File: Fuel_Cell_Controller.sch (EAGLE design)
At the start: 93 parts, among them J1 BLUETOOTH, U1 MAX232PTH

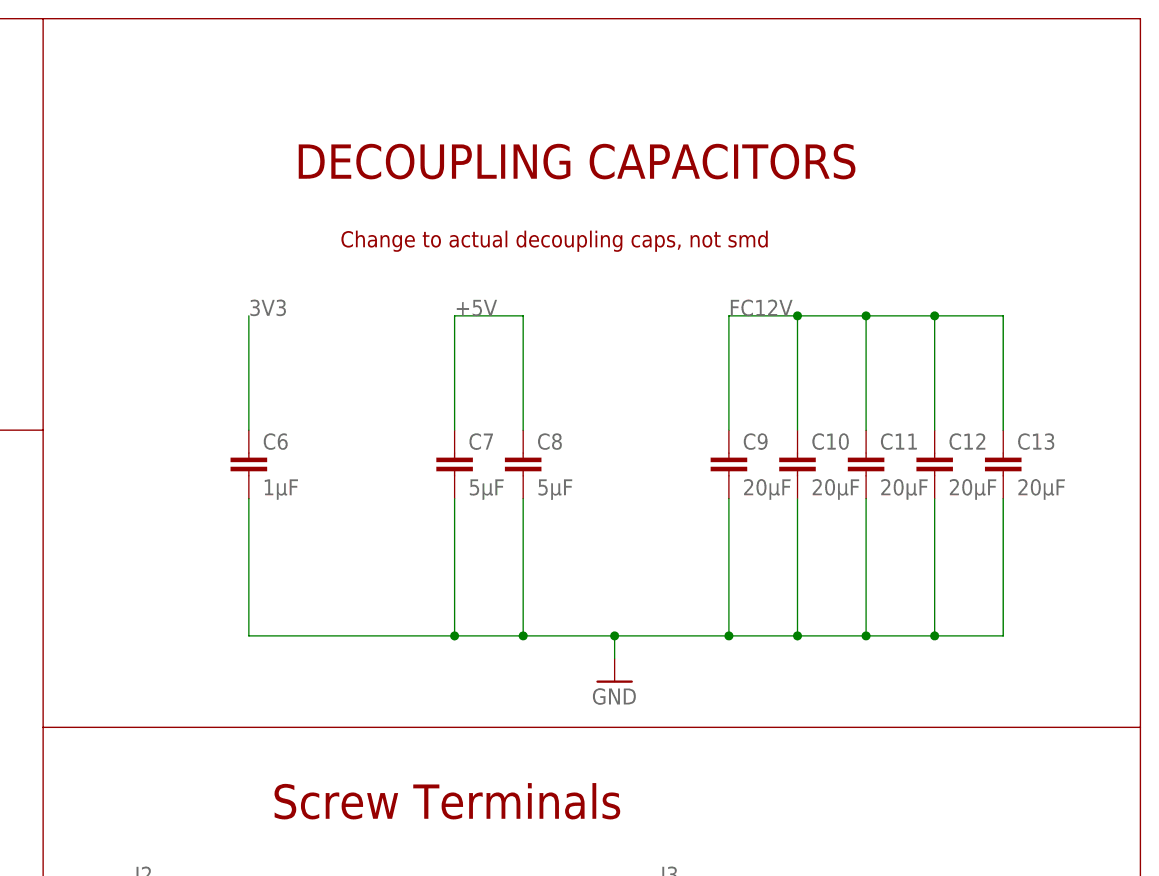
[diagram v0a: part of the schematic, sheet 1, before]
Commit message: Changed the values and number of decoupling capacitors
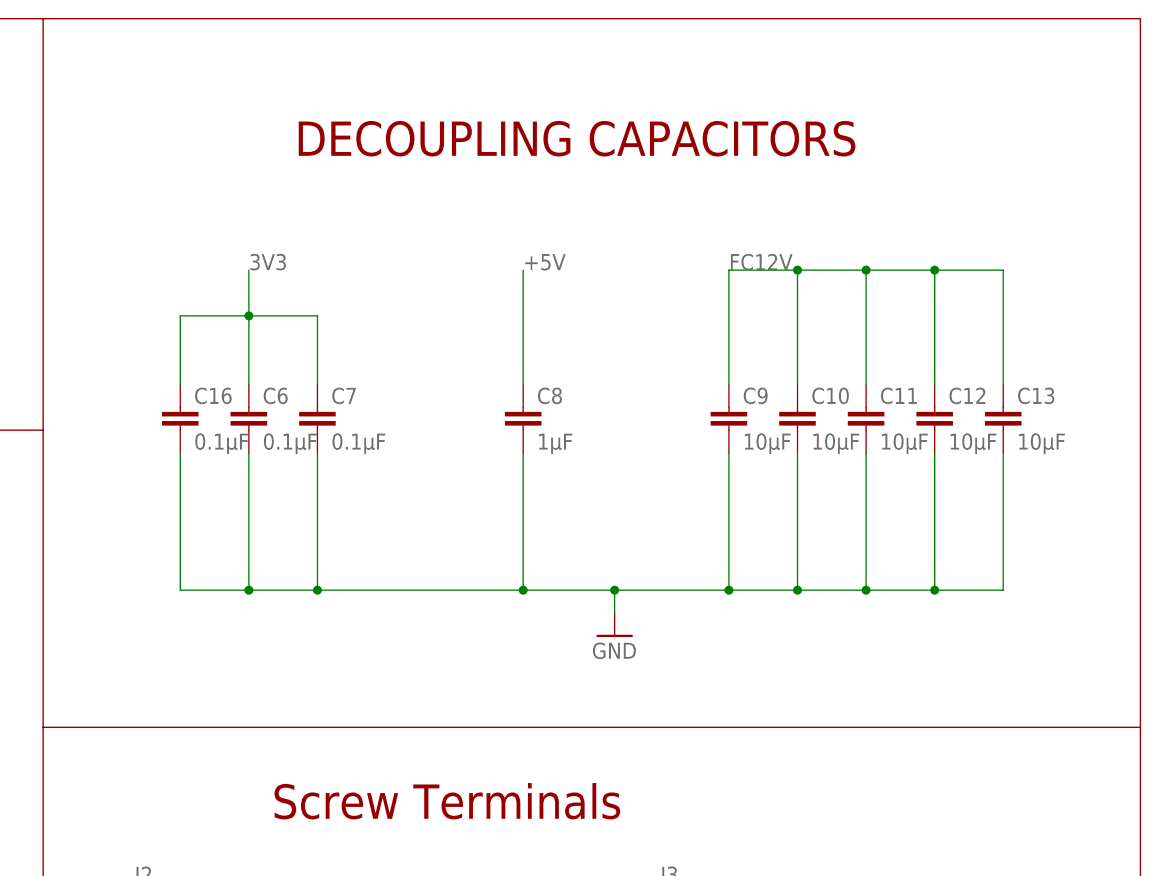
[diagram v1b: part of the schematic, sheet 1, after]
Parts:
- added C16: 0.1µF, SparkFun-Capacitors:CAP0805
- C10, C11, C12, C13, C9: value 20µF -> 10µF; device SparkFun-Capacitors:CAP0603-CAP -> SparkFun-Capacitors:CAP0805
- C6: value 1µF -> 0.1µF; device SparkFun-Capacitors:CAP0603-CAP -> SparkFun-Capacitors:CAP0805
- C7: value 5µF -> 0.1µF; device SparkFun-Capacitors:CAP0603-CAP -> SparkFun-Capacitors:CAP0805
- C8: value 5µF -> 1µF; device SparkFun-Capacitors:CAP0603-CAP -> SparkFun-Capacitors:CAP0805
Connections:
- net +5V: no longer C7.1
- net 3V3: now also C16.1, C7.1
- net GND: now also C16.2
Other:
- note removed: "Change to actual decoupling caps, not smd"
- moved on the sheet: C10, C11, C12, C13, C6, C7, C8, C9

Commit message: Added push button
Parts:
- added R24: 10kΩ, SparkFun-Passives:RESISTOR0805-RES
- added U$26: EG4621CT-ND, EG4621CT-ND:EG4621CT-ND
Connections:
- new net BUTTON: R24.2, U$1.PF_2, U$26.P$2
- net 3V3: now also U$26.P$1
- net GND: now also R24.1
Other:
- note added: "PUSH BUTTON (ACTIVE HIGH)"
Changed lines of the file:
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@@
 <part name="C7" library="SparkFun-Capacitors" deviceset="CAP" device="0805" value="0.1µF"/>
 <part name="C16" library="SparkFun-Capacitors" deviceset="CAP" device="0805" value="0.1µF"/>
+<part name="U$26" library="EG4621CT-ND" deviceset="EG4621CT-ND" device=""/>
+<part name="R24" library="SparkFun-Passives" deviceset="RESISTOR" device="0805-RES" value="10kΩ"/>
 </parts>
 <sheets>
@@
 <wire x1="256.54" y1="-180.34" x2="256.54" y2="-96.52" width="0.1524" layer="94"/>
 <text x="287.02" y="-147.32" size="3.81" layer="94">Indicator LED's</text>
-<wire x1="360.68" y1="-215.9" x2="360.68" y2="-137.16" width="0.1524" layer="94"/>
+<wire x1="360.68" y1="-215.9" x2="360.68" y2="-172.72" width="0.1524" layer="94"/>
+<wire x1="360.68" y1="-172.72" x2="360.68" y2="-137.16" width="0.1524" layer="94"/>
 <wire x1="-93.98" y1="-208.28" x2="-93.98" y2="-259.08" width="0.1524" layer="94"/>
 <wire x1="-93.98" y1="-259.08" x2="124.46" y2="-259.08" width="0.1524" layer="94"/>
@@
 <wire x1="482.6" y1="-45.72" x2="482.6" y2="-127" width="0.1524" layer="94"/>
 <wire x1="482.6" y1="-127" x2="360.68" y2="-127" width="0.1524" layer="94"/>
+<text x="383.54" y="-137.16" size="3.81" layer="94">PUSH BUTTON (ACTIVE HIGH)</text>
+<wire x1="360.68" y1="-172.72" x2="482.6" y2="-172.72" width="0.1524" layer="94"/>
+<wire x1="482.6" y1="-172.72" x2="482.6" y2="-127" width="0.1524" layer="94"/>
 </plain>
 <instances>
@@
 <instance part="C7" gate="G$1" x="391.16" y="33.02"/>
 <instance part="C16" gate="G$1" x="375.92" y="33.02"/>
+<instance part="U$26" gate="G$1" x="408.94" y="-154.94"/>
+<instance part="R24" gate="G$1" x="411.48" y="-162.56"/>
 </instances>
 <busses>
@@
 <label x="447.04" y="-30.48" size="1.778" layer="95"/>
 </segment>
+<segment>
+<pinref part="R24" gate="G$1" pin="1"/>
+<wire x1="406.4" y1="-162.56" x2="388.62" y2="-162.56" width="0.1524" layer="91"/>
+<label x="388.62" y="-162.56" size="1.778" layer="95"/>
+</segment>
 </net>
 <net name="+5V" class="0">
@@
 <pinref part="R16" gate="G$1" pin="1"/>
 <wire x1="-50.8" y1="-165.1" x2="-38.1" y2="-165.1" width="0.1524" layer="91"/>
+</segment>
+<segment>
+<pinref part="U$26" gate="G$1" pin="P$1"/>
+<wire x1="401.32" y1="-154.94" x2="388.62" y2="-154.94" width="0.1524" layer="91"/>
+<label x="388.62" y="-154.94" size="1.778" layer="95"/>
 </segment>
 </net>
@@
 </segment>
 </net>
+<net name="BUTTON" class="0">
+<segment>
+<pinref part="U$26" gate="G$1" pin="P$2"/>
+<label x="424.18" y="-154.94" size="1.778" layer="95"/>
+<wire x1="416.56" y1="-154.94" x2="419.1" y2="-154.94" width="0.1524" layer="91"/>
+<pinref part="R24" gate="G$1" pin="2"/>
+<wire x1="419.1" y1="-154.94" x2="429.26" y2="-154.94" width="0.1524" layer="91"/>
+<wire x1="419.1" y1="-154.94" x2="419.1" y2="-162.56" width="0.1524" layer="91"/>
+<wire x1="419.1" y1="-162.56" x2="416.56" y2="-162.56" width="0.1524" layer="91"/>
+<junction x="419.1" y="-154.94"/>
+</segment>
+<segment>
+<pinref part="U$1" gate="G$1" pin="PF_2"/>
+<wire x1="88.9" y1="-17.78" x2="109.22" y2="-17.78" width="0.1524" layer="91"/>
+<label x="104.14" y="-17.78" size="1.778" layer="95"/>
+</segment>
+</net>

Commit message: Added electrolytic decoupling capacitors and start signal
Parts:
- added ETH9: ETHERNET, ETHERNET:ETHERNET
- added JP4: (no value), jumper:JP1E
- added U$27, U$28: 1µF, 100uF_Cap:CAP-VS-SERIES-PACKAGE-E(ELECT)VS-SERIES-PACKAGE-E
- added U$29: 10µF, 100uF_Cap:CAP-VS-SERIES-PACKAGE-E(ELECT)VS-SERIES-PACKAGE-E
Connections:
- new net START: J3.5, JP4.2
- new net _START: ETH9.1, JP4.1, U$1.PF_12(D8)
- net +5V: now also U$28.+
- net 3V3: now also U$27.+
- net FC12V: now also U$29.+
- net GND: now also ETH9.8, ETH9.SHD1, ETH9.SHD2, U$27.-, U$28.-, U$29.-
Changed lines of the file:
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@@
 <part name="U$26" library="EG4621CT-ND" deviceset="EG4621CT-ND" device=""/>
 <part name="R24" library="SparkFun-Passives" deviceset="RESISTOR" device="0805-RES" value="10kΩ"/>
+<part name="U$27" library="100uF_Cap" deviceset="CAP-VS-SERIES-PACKAGE-E(ELECT)" device="VS-SERIES-PACKAGE-E" value="1µF"/>
+<part name="U$28" library="100uF_Cap" deviceset="CAP-VS-SERIES-PACKAGE-E(ELECT)" device="VS-SERIES-PACKAGE-E" value="1µF"/>
+<part name="U$29" library="100uF_Cap" deviceset="CAP-VS-SERIES-PACKAGE-E(ELECT)" device="VS-SERIES-PACKAGE-E" value="10µF"/>
+<part name="JP4" library="jumper" library_urn="urn:adsk.eagle:library:252" deviceset="JP1E" device="" package3d_urn="urn:adsk.eagle:package:15455/1"/>
+<part name="ETH9" library="ETHERNET" deviceset="ETHERNET" device=""/>
 </parts>
 <sheets>
@@
 <instance part="U$26" gate="G$1" x="408.94" y="-154.94"/>
 <instance part="R24" gate="G$1" x="411.48" y="-162.56"/>
+<instance part="U$27" gate="G$1" x="398.78" y="35.56"/>
+<instance part="U$28" gate="G$1" x="421.64" y="35.56"/>
+<instance part="U$29" gate="G$1" x="474.98" y="35.56"/>
+<instance part="JP4" gate="A" x="421.64" y="-40.64" rot="R90"/>
 </instances>
 <busses>
@@
 <wire x1="467.36" y1="30.48" x2="467.36" y2="15.24" width="0.1524" layer="91"/>
 <wire x1="383.54" y1="15.24" x2="391.16" y2="15.24" width="0.1524" layer="91"/>
-<wire x1="391.16" y1="15.24" x2="414.02" y2="15.24" width="0.1524" layer="91"/>
-<wire x1="414.02" y1="15.24" x2="424.18" y2="15.24" width="0.1524" layer="91"/>
+<wire x1="391.16" y1="15.24" x2="398.78" y2="15.24" width="0.1524" layer="91"/>
+<wire x1="398.78" y1="15.24" x2="414.02" y2="15.24" width="0.1524" layer="91"/>
+<wire x1="414.02" y1="15.24" x2="421.64" y2="15.24" width="0.1524" layer="91"/>
+<wire x1="421.64" y1="15.24" x2="424.18" y2="15.24" width="0.1524" layer="91"/>
 <wire x1="424.18" y1="15.24" x2="436.88" y2="15.24" width="0.1524" layer="91"/>
 <wire x1="436.88" y1="15.24" x2="444.5" y2="15.24" width="0.1524" layer="91"/>
@@
 <wire x1="375.92" y1="15.24" x2="375.92" y2="30.48" width="0.1524" layer="91"/>
 <junction x="383.54" y="15.24"/>
+<pinref part="U$27" gate="G$1" pin="-"/>
+<wire x1="398.78" y1="30.48" x2="398.78" y2="15.24" width="0.1524" layer="91"/>
+<junction x="398.78" y="15.24"/>
+<pinref part="U$28" gate="G$1" pin="-"/>
+<wire x1="421.64" y1="30.48" x2="421.64" y2="15.24" width="0.1524" layer="91"/>
+<junction x="421.64" y="15.24"/>
+<pinref part="U$29" gate="G$1" pin="-"/>
+<wire x1="474.98" y1="30.48" x2="474.98" y2="15.24" width="0.1524" layer="91"/>
+<wire x1="474.98" y1="15.24" x2="467.36" y2="15.24" width="0.1524" layer="91"/>
+<junction x="467.36" y="15.24"/>
 </segment>
 <segment>
@@
 <segment>
 <pinref part="C8" gate="G$1" pin="1"/>
-<wire x1="414.02" y1="38.1" x2="414.02" y2="50.8" width="0.1524" layer="91"/>
+<wire x1="414.02" y1="38.1" x2="414.02" y2="45.72" width="0.1524" layer="91"/>
 <label x="414.02" y="50.8" size="1.778" layer="95"/>
+<pinref part="U$28" gate="G$1" pin="+"/>
+<wire x1="414.02" y1="45.72" x2="414.02" y2="50.8" width="0.1524" layer="91"/>
+<wire x1="414.02" y1="45.72" x2="421.64" y2="45.72" width="0.1524" layer="91"/>
+<wire x1="421.64" y1="45.72" x2="421.64" y2="38.1" width="0.1524" layer="91"/>
+<junction x="414.02" y="45.72"/>
 </segment>
 <segment>
@@
 <wire x1="383.54" y1="45.72" x2="391.16" y2="45.72" width="0.1524" layer="91"/>
 <wire x1="391.16" y1="45.72" x2="391.16" y2="38.1" width="0.1524" layer="91"/>
+<pinref part="U$27" gate="G$1" pin="+"/>
+<wire x1="391.16" y1="45.72" x2="398.78" y2="45.72" width="0.1524" layer="91"/>
+<wire x1="398.78" y1="45.72" x2="398.78" y2="38.1" width="0.1524" layer="91"/>
+<junction x="391.16" y="45.72"/>
 </segment>
 <segment>
@@
 <junction x="444.5" y="50.8"/>
 <label x="436.88" y="50.8" size="1.778" layer="95"/>
+<pinref part="U$29" gate="G$1" pin="+"/>
+<wire x1="467.36" y1="50.8" x2="474.98" y2="50.8" width="0.1524" layer="91"/>
+<wire x1="474.98" y1="50.8" x2="474.98" y2="38.1" width="0.1524" layer="91"/>
+<junction x="467.36" y="50.8"/>
 </segment>
 </net>
@@
 <wire x1="88.9" y1="-17.78" x2="109.22" y2="-17.78" width="0.1524" layer="91"/>
 <label x="104.14" y="-17.78" size="1.778" layer="95"/>
+</segment>
+</net>
+<net name="START" class="0">
+<segment>
+<pinref part="J3" gate="G$1" pin="5"/>
+<wire x1="439.42" y1="-20.32" x2="452.12" y2="-20.32" width="0.1524" layer="91"/>
+<label x="447.04" y="-20.32" size="1.778" layer="95"/>
+</segment>
+<segment>
+<pinref part="JP4" gate="A" pin="2"/>
+<wire x1="424.18" y1="-38.1" x2="436.88" y2="-38.1" width="0.1524" layer="91"/>
+<label x="431.8" y="-38.1" size="1.778" layer="95"/>
+</segment>
+</net>
+<net name="_START" class="0">
+<segment>
+<pinref part="JP4" gate="A" pin="1"/>
+<wire x1="424.18" y1="-40.64" x2="436.88" y2="-40.64" width="0.1524" layer="91"/>
+<label x="431.8" y="-40.64" size="1.778" layer="95"/>
+</segment>
+<segment>
+<pinref part="U$1" gate="G$1" pin="PF_12(D8)"/>
+<wire x1="88.9" y1="-38.1" x2="109.22" y2="-38.1" width="0.1524" layer="91"/>
+<label x="104.14" y="-38.1" size="1.778" layer="95"/>
 </segment>
 </net>
@@
 <text x="-15.24" y="215.9" size="1.778" layer="94">ETHERNET CONNECTORS</text>
 <text x="99.06" y="215.9" size="1.778" layer="94">POWER CONNECTORS</text>
-<wire x1="-15.24" y1="213.36" x2="-15.24" y2="-127" width="0.1524" layer="94"/>
-<wire x1="-15.24" y1="-127" x2="86.36" y2="-127" width="0.1524" layer="94"/>
-<wire x1="86.36" y1="-127" x2="86.36" y2="213.36" width="0.1524" layer="94"/>
+<wire x1="-15.24" y1="213.36" x2="-15.24" y2="-200.66" width="0.1524" layer="94"/>
+<wire x1="-15.24" y1="-200.66" x2="86.36" y2="-200.66" width="0.1524" layer="94"/>
+<wire x1="86.36" y1="-200.66" x2="86.36" y2="213.36" width="0.1524" layer="94"/>
 <wire x1="86.36" y1="213.36" x2="-15.24" y2="213.36" width="0.1524" layer="94"/>
 <wire x1="99.06" y1="213.36" x2="223.52" y2="213.36" width="0.1524" layer="94"/>
@@
 <instance part="ETH3" gate="G$1" x="60.96" y="127"/>
 <instance part="ETH1" gate="G$1" x="20.32" y="182.88"/>
+<instance part="ETH9" gate="G$1" x="20.32" y="-154.94"/>
 </instances>
 <busses>
@@
 <label x="2.54" y="68.58" size="1.778" layer="95"/>
 </segment>
+<segment>
+<pinref part="ETH9" gate="G$1" pin="SHD1"/>
+<wire x1="15.24" y1="-170.18" x2="10.16" y2="-170.18" width="0.1524" layer="91"/>
+<wire x1="10.16" y1="-170.18" x2="10.16" y2="-172.72" width="0.1524" layer="91"/>
+<pinref part="ETH9" gate="G$1" pin="SHD2"/>
+<wire x1="10.16" y1="-172.72" x2="10.16" y2="-180.34" width="0.1524" layer="91"/>
+<wire x1="15.24" y1="-172.72" x2="10.16" y2="-172.72" width="0.1524" layer="91"/>
+<junction x="10.16" y="-172.72"/>
+<label x="10.16" y="-180.34" size="1.778" layer="95"/>
+</segment>
+<segment>
+<pinref part="ETH9" gate="G$1" pin="8"/>
+<wire x1="15.24" y1="-157.48" x2="5.08" y2="-157.48" width="0.1524" layer="91"/>
+<label x="5.08" y="-157.48" size="1.778" layer="95"/>
+</segment>
 </net>
 <net name="FC5V" class="0">
@@
 </segment>
 </net>
+<net name="_START" class="0">
+<segment>
+<pinref part="ETH9" gate="G$1" pin="1"/>
+<wire x1="15.24" y1="-139.7" x2="5.08" y2="-139.7" width="0.1524" layer="91"/>
+<label x="5.08" y="-139.7" size="1.778" layer="95"/>
+</segment>
+</net>
